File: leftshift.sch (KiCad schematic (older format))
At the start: 15 parts

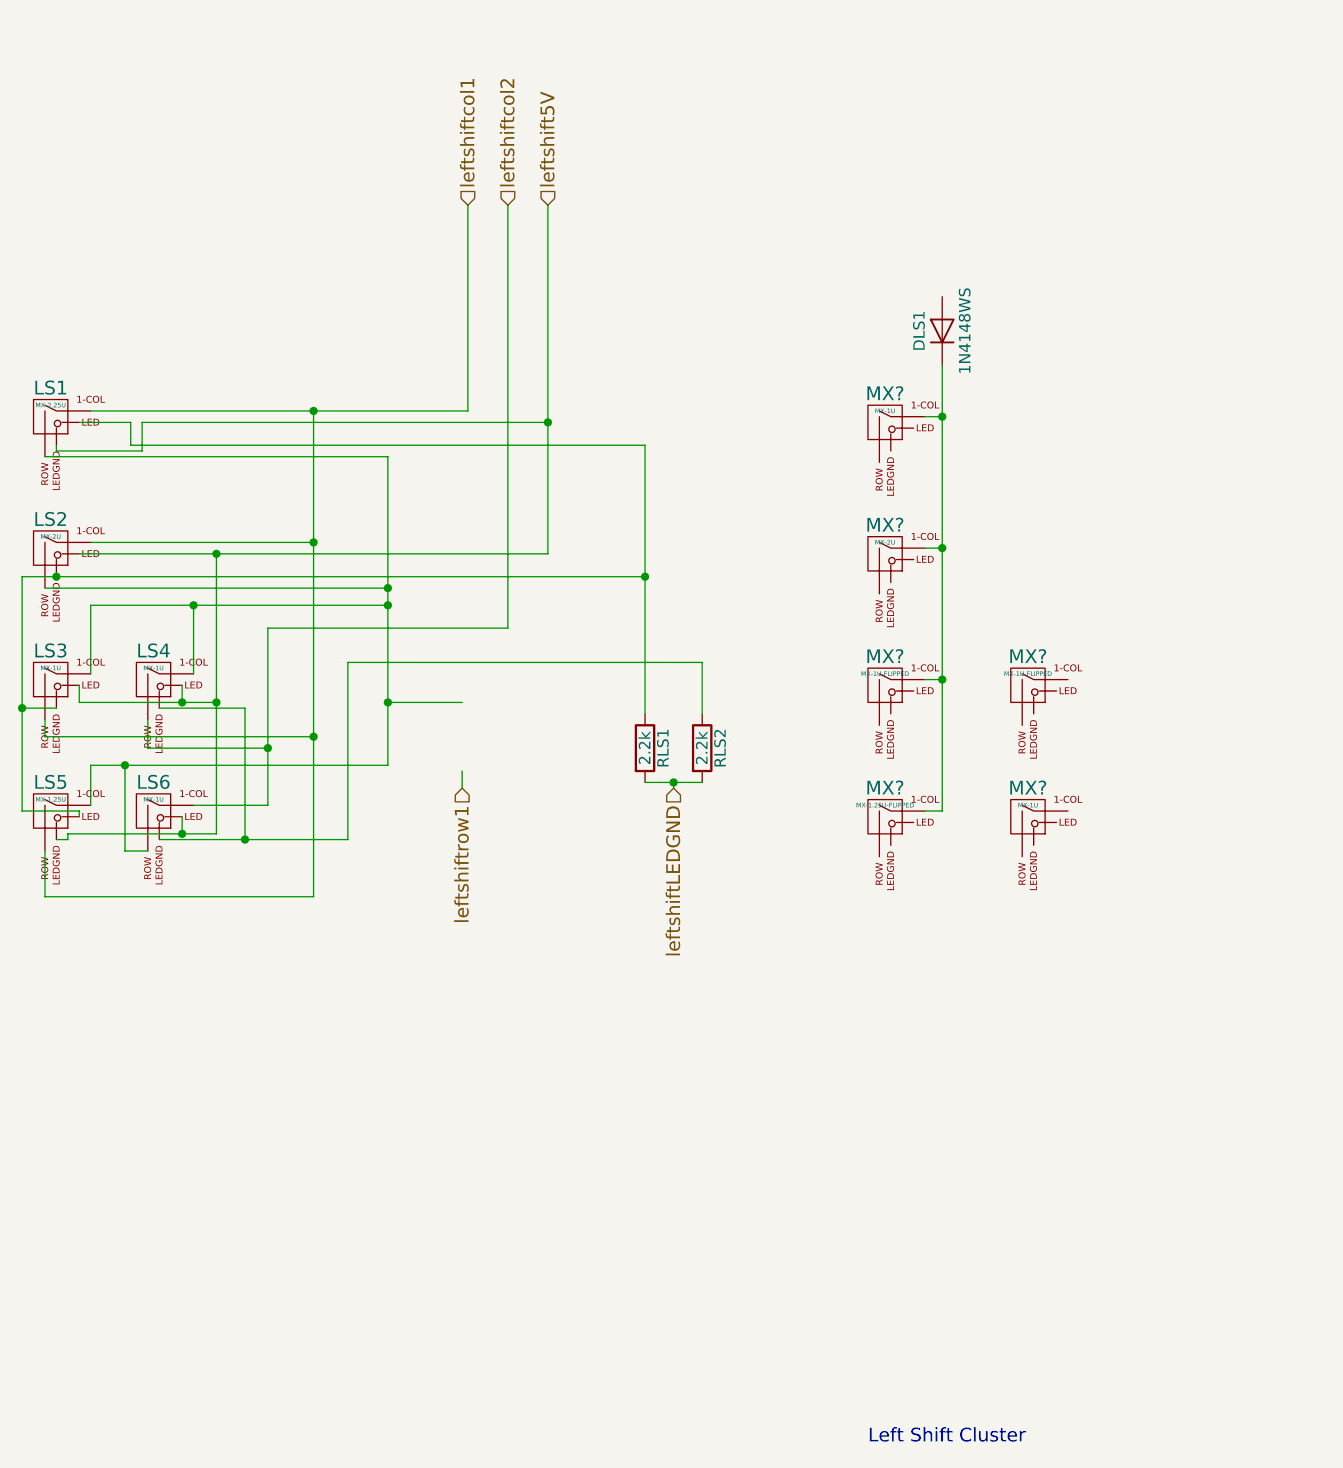
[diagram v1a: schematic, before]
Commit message: Fixed left shift
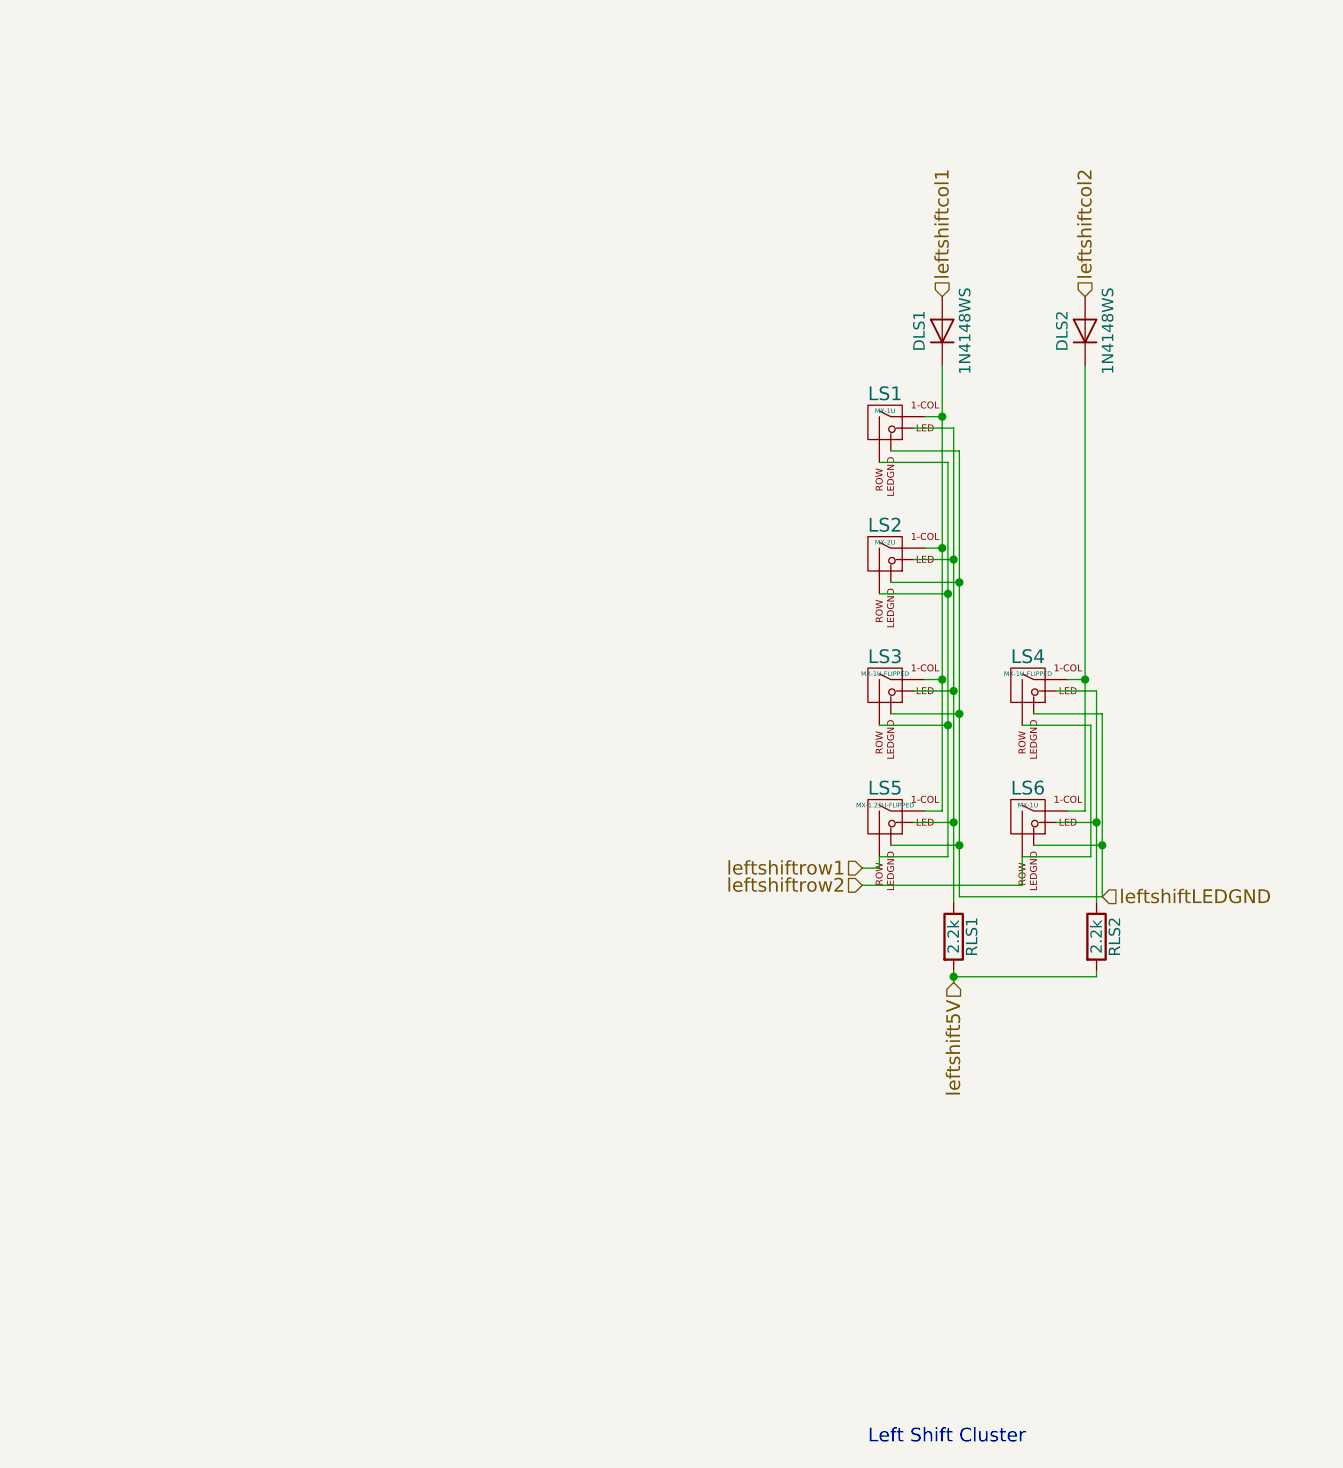
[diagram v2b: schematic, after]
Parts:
- removed LS1: MX-2.25U, symbol MX-2.25U
- removed LS2: MX-2U, symbol MX-2U
- removed LS3, LS4, LS6: MX-1U, symbol MX-1U
- removed LS5: MX-1.25U, symbol MX-1.25U
- added DLS2: 1N4148WS, symbol D
- gave numbers to parts that had none: 6
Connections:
- net labels added: leftshiftrow2
- wire segments 62 -> 55
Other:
- moved on the sheet: RLS1, RLS2

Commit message: Update annotations
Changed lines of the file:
@@
 $Descr A4 11693 8268
 encoding utf-8
-Sheet 1 7
+Sheet 7 7
 Title ""
 Date ""
@@
 $EndComp
 Wire Wire Line
-	7650 2775 7650 3000
-Wire Wire Line
-	7650 3000 7650 3575
-Wire Wire Line
-	7650 3575 7650 4150
-Wire Wire Line
-	7650 4150 7650 4725
+	7650 2775 7650 4725
 Wire Wire Line
 	7650 3000 7575 3000
@@
 	8275 4725 8200 4725
 Wire Wire Line
-	8275 2775 8275 4150
-Wire Wire Line
-	8275 4150 8275 4725
+	8275 2775 8275 4725
 Wire Wire Line
 	8200 4150 8275 4150
@@
 	8300 4925 8000 4925
 Wire Wire Line
-	7375 4350 7675 4350
-Wire Wire Line
-	7675 3200 7675 3775
-Wire Wire Line
-	7675 3775 7675 4350
-Wire Wire Line
-	7675 4350 7675 4925
+	7675 4350 7375 4350
+Wire Wire Line
+	7675 3200 7675 4925
 Wire Wire Line
 	7375 3775 7675 3775
@@
 	7525 3050 7700 3050
 Wire Wire Line
-	7700 3050 7700 3625
-Wire Wire Line
-	7700 3625 7700 4200
-Wire Wire Line
-	7700 4200 7700 4775
-Wire Wire Line
-	7700 4775 7700 5125
+	7700 3050 7700 5125
 Wire Wire Line
 	7700 3625 7525 3625
@@
 	8150 4775 8325 4775
 Wire Wire Line
-	8325 4200 8325 4775
-Wire Wire Line
-	8325 4775 8325 5125
+	8325 4200 8325 5125
 Wire Wire Line
 	8325 4200 8150 4200
@@
 	8050 4300 8350 4300
 Wire Wire Line
-	8350 4300 8350 4875
-Wire Wire Line
-	8350 4875 8350 5100
+	8350 4300 8350 5100
 Wire Wire Line
 	8350 4875 8050 4875
@@
 	7725 4875 7425 4875
 Wire Wire Line
-	7725 3150 7725 3725
-Wire Wire Line
-	7725 3725 7725 4300
-Wire Wire Line
-	7725 4300 7725 4875
-Wire Wire Line
-	7725 4875 7725 5100
+	7725 3150 7725 5100
 Wire Wire Line
 	7725 4300 7425 4300
@@
 Connection ~ 7700 4775
 Wire Wire Line
-	7700 5425 7700 5450
-Wire Wire Line
-	7700 5450 7700 5475
+	7700 5425 7700 5475
 Wire Wire Line
 	7700 5450 8325 5450

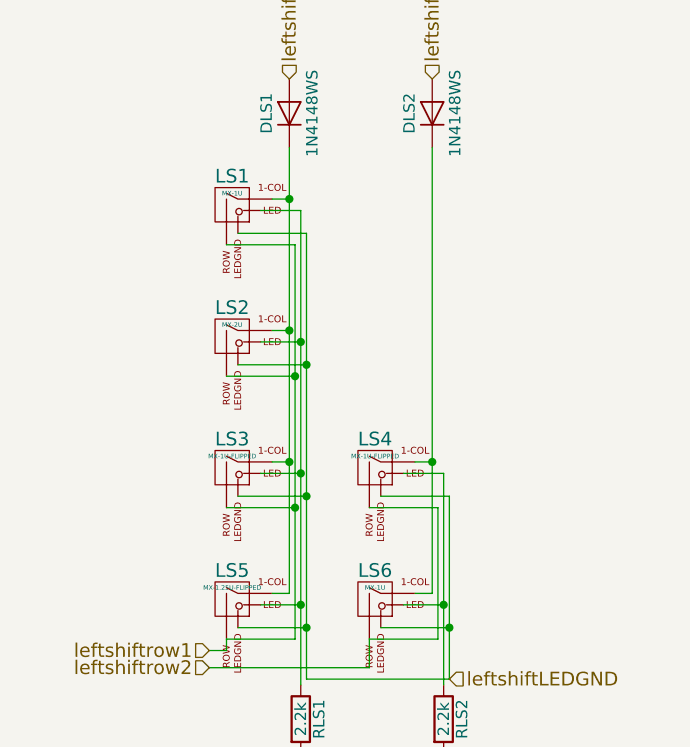
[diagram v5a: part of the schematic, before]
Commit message: Fix all key annotations
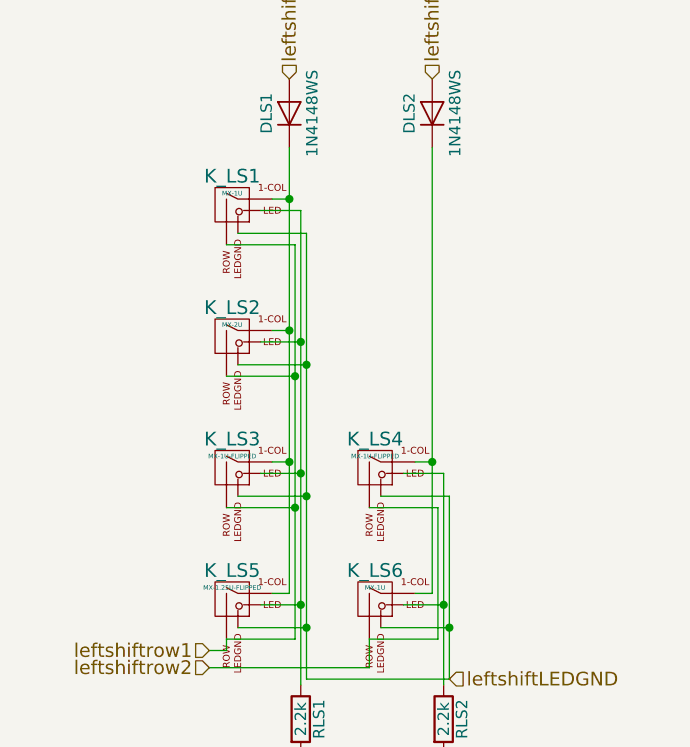
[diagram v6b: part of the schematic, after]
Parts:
- renumbered LS1 to K_LS1, LS2 to K_LS2, LS3 to K_LS3, LS4 to K_LS4, LS5 to K_LS5, LS6 to K_LS6
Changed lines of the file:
@@
 leftshiftLEDGND
 $Comp
-L MX-1U LS1
+L MX-1U K_LS1
 U 1 1 591BDC1C
 P 7400 3025
-F 0 "LS1" H 7400 3150 60  0000 C CNN
+F 0 "K_LS1" H 7400 3150 60  0000 C CNN
 F 1 "MX-1U" H 7400 3075 20  0000 C CNN
 F 2 "" H 7375 3000 60  0001 C CNN
@@
 $EndComp
 $Comp
-L MX-2U LS2
+L MX-2U K_LS2
 U 1 1 591BE12C
 P 7400 3600
-F 0 "LS2" H 7400 3725 60  0000 C CNN
+F 0 "K_LS2" H 7400 3725 60  0000 C CNN
 F 1 "MX-2U" H 7400 3650 20  0000 C CNN
 F 2 "" H 7375 3575 60  0001 C CNN
@@
 $EndComp
 $Comp
-L MX-1U-FLIPPED LS4
+L MX-1U-FLIPPED K_LS4
 U 1 1 591C1993
 P 8025 4175
-F 0 "LS4" H 8025 4300 60  0000 C CNN
+F 0 "K_LS4" H 8025 4300 60  0000 C CNN
 F 1 "MX-1U-FLIPPED" H 8025 4225 20  0000 C CNN
 F 2 "" H 8000 4150 60  0001 C CNN
@@
 $EndComp
 $Comp
-L MX-1U-FLIPPED LS3
+L MX-1U-FLIPPED K_LS3
 U 1 1 591BFCFF
 P 7400 4175
-F 0 "LS3" H 7400 4300 60  0000 C CNN
+F 0 "K_LS3" H 7400 4300 60  0000 C CNN
 F 1 "MX-1U-FLIPPED" H 7400 4225 20  0000 C CNN
 F 2 "" H 7375 4150 60  0001 C CNN
@@
 $EndComp
 $Comp
-L MX-1.25U-FLIPPED LS5
+L MX-1.25U-FLIPPED K_LS5
 U 1 1 591C5253
 P 7400 4750
-F 0 "LS5" H 7400 4875 60  0000 C CNN
+F 0 "K_LS5" H 7400 4875 60  0000 C CNN
 F 1 "MX-1.25U-FLIPPED" H 7400 4800 20  0000 C CNN
 F 2 "" H 7375 4725 60  0001 C CNN
@@
 $EndComp
 $Comp
-L MX-1U LS6
+L MX-1U K_LS6
 U 1 1 591C67D6
 P 8025 4750
-F 0 "LS6" H 8025 4875 60  0000 C CNN
+F 0 "K_LS6" H 8025 4875 60  0000 C CNN
 F 1 "MX-1U" H 8025 4800 20  0000 C CNN
 F 2 "" H 8000 4725 60  0001 C CNN

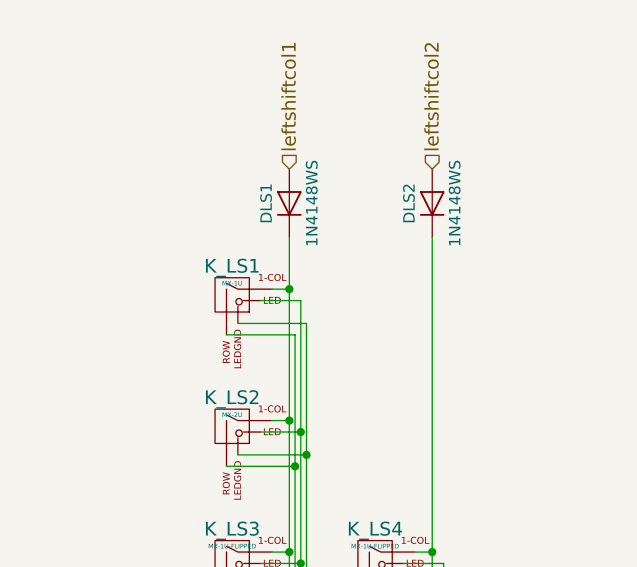
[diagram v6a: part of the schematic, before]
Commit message: Fix left shift, associate MX footprints
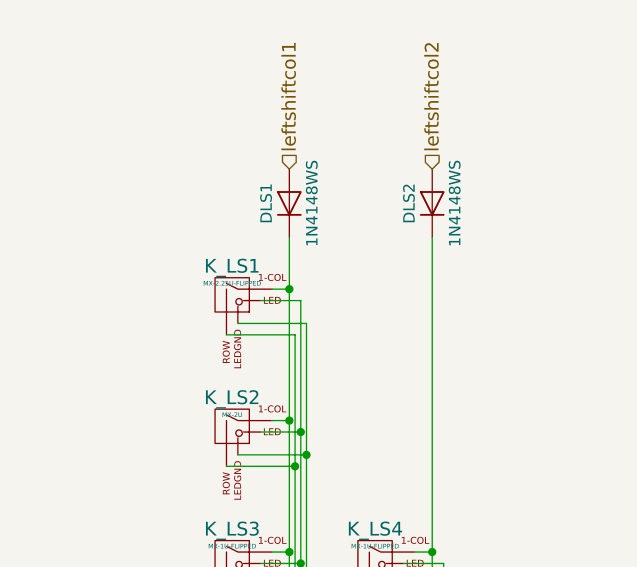
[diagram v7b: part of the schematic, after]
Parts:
- removed K_LS1: MX-1U, symbol MX-1U
- added K_LS1: MX-2.25U-FLIPPED, symbol MX-2.25U-FLIPPED
- K_LS2: footprint (none) -> MX_Alps_Hybrid:MX-2U
- K_LS3, K_LS4, K_LS6: footprint (none) -> MX_Alps_Hybrid:MX-1U
- K_LS5: footprint (none) -> MX_Alps_Hybrid:MX-1.25U
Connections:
- net leftshiftLEDGND: now also K_LS1.4 (LEDGND)
- net leftshiftrow1: now also K_LS1.1 (ROW)
- net at DLS1.1 (K), K_LS2.1 (COL), K_LS3.2 (COL)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: now also K_LS1.2 (COL)
- net at K_LS2.3 (LED), K_LS3.3 (LED), K_LS5.3 (LED)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: now also K_LS1.3 (LED)
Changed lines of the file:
@@
 leftshiftLEDGND
-$Comp
-L MX-1U K_LS1
-U 1 1 591BDC1C
-P 7400 3025
-F 0 "K_LS1" H 7400 3150 60  0000 C CNN
-F 1 "MX-1U" H 7400 3075 20  0000 C CNN
-F 2 "" H 7375 3000 60  0001 C CNN
-F 3 "" H 7375 3000 60  0001 C CNN
-	1    7400 3025
-	1    0    0    -1
-$EndComp
 $Comp
 L MX-2U K_LS2
@@
 F 0 "K_LS2" H 7400 3725 60  0000 C CNN
 F 1 "MX-2U" H 7400 3650 20  0000 C CNN
-F 2 "" H 7375 3575 60  0001 C CNN
+F 2 "MX_Alps_Hybrid:MX-2U" H 7375 3575 60  0001 C CNN
 F 3 "" H 7375 3575 60  0001 C CNN
 	1    7400 3600
@@
 F 0 "K_LS4" H 8025 4300 60  0000 C CNN
 F 1 "MX-1U-FLIPPED" H 8025 4225 20  0000 C CNN
-F 2 "" H 8000 4150 60  0001 C CNN
+F 2 "MX_Alps_Hybrid:MX-1U" H 8000 4150 60  0001 C CNN
 F 3 "" H 8000 4150 60  0001 C CNN
 	1    8025 4175
@@
 F 0 "K_LS3" H 7400 4300 60  0000 C CNN
 F 1 "MX-1U-FLIPPED" H 7400 4225 20  0000 C CNN
-F 2 "" H 7375 4150 60  0001 C CNN
+F 2 "MX_Alps_Hybrid:MX-1U" H 7375 4150 60  0001 C CNN
 F 3 "" H 7375 4150 60  0001 C CNN
 	1    7400 4175
@@
 F 0 "K_LS5" H 7400 4875 60  0000 C CNN
 F 1 "MX-1.25U-FLIPPED" H 7400 4800 20  0000 C CNN
-F 2 "" H 7375 4725 60  0001 C CNN
+F 2 "MX_Alps_Hybrid:MX-1.25U" H 7375 4725 60  0001 C CNN
 F 3 "" H 7375 4725 60  0001 C CNN
 	1    7400 4750
@@
 F 0 "K_LS6" H 8025 4875 60  0000 C CNN
 F 1 "MX-1U" H 8025 4800 20  0000 C CNN
-F 2 "" H 8000 4725 60  0001 C CNN
+F 2 "MX_Alps_Hybrid:MX-1U" H 8000 4725 60  0001 C CNN
 F 3 "" H 8000 4725 60  0001 C CNN
 	1    8025 4750
@@
 Text HLabel 7650 2475 1    60   Input ~ 0
 leftshiftcol1
+$Comp
+L MX-2.25U-FLIPPED K_LS1
+U 1 1 5947D05F
+P 7400 3025
+F 0 "K_LS1" H 7400 3150 60  0000 C CNN
+F 1 "MX-2.25U-FLIPPED" H 7400 3075 20  0000 C CNN
+F 2 "" H 7375 3000 60  0001 C CNN
+F 3 "" H 7375 3000 60  0001 C CNN
+	1    7400 3025
+	1    0    0    -1
+$EndComp
 $EndSCHEMATC

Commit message: Row 3
We're missing 1.25U for split enter
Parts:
- K_LS1: footprint (none) -> MX_Alps_Hybrid:MX-2.25U
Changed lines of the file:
@@
 F 0 "K_LS1" H 7400 3150 60  0000 C CNN
 F 1 "MX-2.25U-FLIPPED" H 7400 3075 20  0000 C CNN
-F 2 "" H 7375 3000 60  0001 C CNN
+F 2 "MX_Alps_Hybrid:MX-2.25U" H 7375 3000 60  0001 C CNN
 F 3 "" H 7375 3000 60  0001 C CNN
 	1    7400 3025
